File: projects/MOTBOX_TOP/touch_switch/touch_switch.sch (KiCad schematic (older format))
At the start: 5 parts, among them J1 Conn_01x03, J2 Conn_01x04, J3 JST_Female_3pin

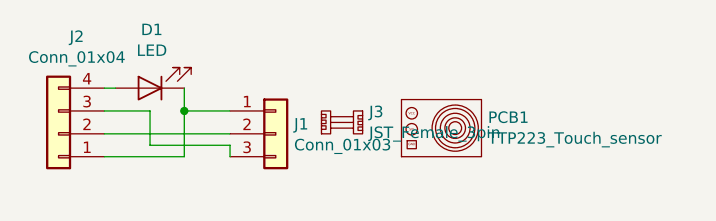
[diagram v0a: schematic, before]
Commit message: New library files and schematics with ESE31 and DT045 switches
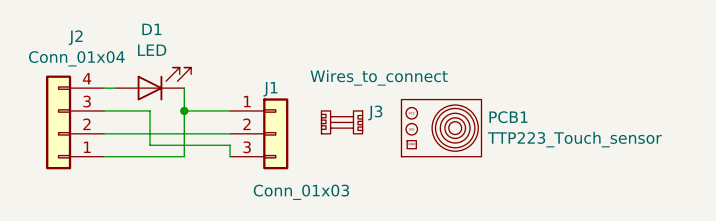
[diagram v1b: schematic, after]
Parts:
- J3: value JST_Female_3pin -> Wires_to_connect
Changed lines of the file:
@@
 U 1 1 5CC06330
 P 5400 3200
-F 0 "J1" H 5480 3242 50  0000 L CNN
-F 1 "Conn_01x03" H 5480 3151 50  0000 L CNN
+F 0 "J1" H 5350 3400 50  0000 L CNN
+F 1 "Conn_01x03" H 5300 2950 50  0000 L CNN
 F 2 "Connector_Wire:SolderWirePad_1x03_P3.175mm_Drill0.8mm" H 5400 3200 50  0001 C CNN
 F 3 "~" H 5400 3200 50  0001 C CNN
@@
 P 5500 3200
 F 0 "J3" H 5808 3296 50  0000 L CNN
-F 1 "JST_Female_3pin" H 5808 3205 50  0000 L CNN
+F 1 "Wires_to_connect" H 5550 3450 50  0000 L CNN
 F 2 "" H 5500 3200 50  0001 C CNN
 F 3 "" H 5500 3200 50  0001 C CNN

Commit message: Touch switch changes for dual color led
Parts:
- removed D1: LED, LED_THT:LED_D3.0mm, symbol Device:LED
- added D1: LED_Dual_ACA, LED_THT:LED_D3.0mm-3, symbol Device:LED_Dual_ACA
- added R1, R2: 150R, Resistor_SMD:R_1206_3216Metric, symbol Device:R_US
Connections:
- wire segments 10 -> 15
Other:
- moved on the sheet: J2
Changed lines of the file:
@@
 $EndDescr
-$Comp
-L Connector_Generic:Conn_01x03 J1
-U 1 1 5CC06330
-P 5400 3200
-F 0 "J1" H 5350 3400 50  0000 L CNN
-F 1 "Conn_01x03" H 5300 2950 50  0000 L CNN
-F 2 "Connector_Wire:SolderWirePad_1x03_P3.175mm_Drill0.8mm" H 5400 3200 50  0001 C CNN
-F 3 "~" H 5400 3200 50  0001 C CNN
-	1    5400 3200
-	1    0    0    -1
-$EndComp
-$Comp
-L Device:LED D1
-U 1 1 5CC063D7
-P 4850 3000
-F 0 "D1" H 4842 2745 50  0000 C CNN
-F 1 "LED" H 4842 2836 50  0000 C CNN
-F 2 "LED_THT:LED_D3.0mm" H 4850 3000 50  0001 C CNN
-F 3 "~" H 4850 3000 50  0001 C CNN
-	1    4850 3000
-	-1   0    0    1
-$EndComp
 $Comp
 L Connector_Generic:Conn_01x04 J2
 U 1 1 5CC28BDB
-P 4450 3200
-F 0 "J2" H 4370 2775 50  0000 C CNN
-F 1 "Conn_01x04" H 4370 2866 50  0000 C CNN
-F 2 "Connector_Wire:SolderWirePad_1x04_P3.175mm_Drill0.8mm" H 4450 3200 50  0001 C CNN
-F 3 "~" H 4450 3200 50  0001 C CNN
-	1    4450 3200
+P 4050 3200
+F 0 "J2" H 3970 2775 50  0000 C CNN
+F 1 "Conn_01x04" H 3970 2866 50  0000 C CNN
+F 2 "Connector_Wire:SolderWirePad_1x04_P3.175mm_Drill0.8mm" H 4050 3200 50  0001 C CNN
+F 3 "~" H 4050 3200 50  0001 C CNN
+	1    4050 3200
 	-1   0    0    1
 $EndComp
-Wire Wire Line
-	4650 3300 5000 3300
-Wire Wire Line
-	4650 3000 4700 3000
-Wire Wire Line
-	5000 3000 5000 3100
 $Comp
 L hitesh_custom:TTP223_Touch_sensor PCB1
@@
 	1    0    0    -1
 $EndComp
+$Comp
+L Device:LED_Dual_ACA D1
+U 1 1 5CF9F500
+P 4900 4200
+F 0 "D1" V 4946 3990 50  0000 R CNN
+F 1 "LED_Dual_ACA" V 4855 3990 50  0000 R CNN
+F 2 "LED_THT:LED_D3.0mm-3" H 4900 4200 50  0001 C CNN
+F 3 "~" H 4900 4200 50  0001 C CNN
+	1    4900 4200
+	0    -1   -1   0
+$EndComp
+$Comp
+L Device:R_US R1
+U 1 1 5CF9F5F0
+P 4800 3650
+F 0 "R1" H 4700 3850 50  0000 L CNN
+F 1 "150R" V 4700 3550 50  0000 L CNN
+F 2 "Resistor_SMD:R_1206_3216Metric" V 4840 3640 50  0001 C CNN
+F 3 "~" H 4800 3650 50  0001 C CNN
+	1    4800 3650
+	1    0    0    -1
+$EndComp
+$Comp
+L Device:R_US R2
+U 1 1 5CF9F9D8
+P 5000 3650
+F 0 "R2" H 5050 3850 50  0000 L CNN
+F 1 "150R" V 5100 3550 50  0000 L CNN
+F 2 "Resistor_SMD:R_1206_3216Metric" V 5040 3640 50  0001 C CNN
+F 3 "~" H 5000 3650 50  0001 C CNN
+	1    5000 3650
+	1    0    0    -1
+$EndComp
 Wire Wire Line
-	5000 3100 5200 3100
-Connection ~ 5000 3100
+	4800 3000 4800 3500
 Wire Wire Line
-	5000 3100 5000 3300
+	5100 3400 5000 3400
 Wire Wire Line
-	4650 3100 4850 3100
+	5000 3400 5000 3500
 Wire Wire Line
-	4850 3100 4850 3250
+	5000 3800 5000 3900
 Wire Wire Line
-	4850 3250 5200 3250
+	4800 3800 4800 3900
 Wire Wire Line
-	5200 3250 5200 3300
+	4250 3300 4350 3300
 Wire Wire Line
-	4650 3200 5200 3200
+	4250 3200 5200 3200
+Wire Wire Line
+	4250 3000 4800 3000
+Wire Wire Line
+	4350 3300 4350 4750
+Wire Wire Line
+	4350 4750 4900 4750
+Wire Wire Line
+	4900 4750 4900 4500
+Connection ~ 4350 3300
+$Comp
+L Connector_Generic:Conn_01x03 J1
+U 1 1 5CC06330
+P 5400 3200
+F 0 "J1" H 5350 3400 50  0000 L CNN
+F 1 "Conn_01x03" H 5300 2950 50  0000 L CNN
+F 2 "Connector_Wire:SolderWirePad_1x03_P3.175mm_Drill0.8mm" H 5400 3200 50  0001 C CNN
+F 3 "~" H 5400 3200 50  0001 C CNN
+	1    5400 3200
+	1    0    0    -1
+$EndComp
+Wire Wire Line
+	4250 3100 5100 3100
+Wire Wire Line
+	4350 3300 5200 3300
+Wire Wire Line
+	5100 3100 5100 3400
+Connection ~ 5100 3100
+Wire Wire Line
+	5100 3100 5200 3100
 $EndSCHEMATC
